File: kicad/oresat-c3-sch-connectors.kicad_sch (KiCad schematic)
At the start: 29 parts, among them J1 J-SAMTEC-TFM-120-01-L-D-RA, J2 J-TE-Debug-2-1734592-0, J3 J-MOLEX-SMPM-73300-003X, J4 J-MOLEX-SMPM-73300-003X

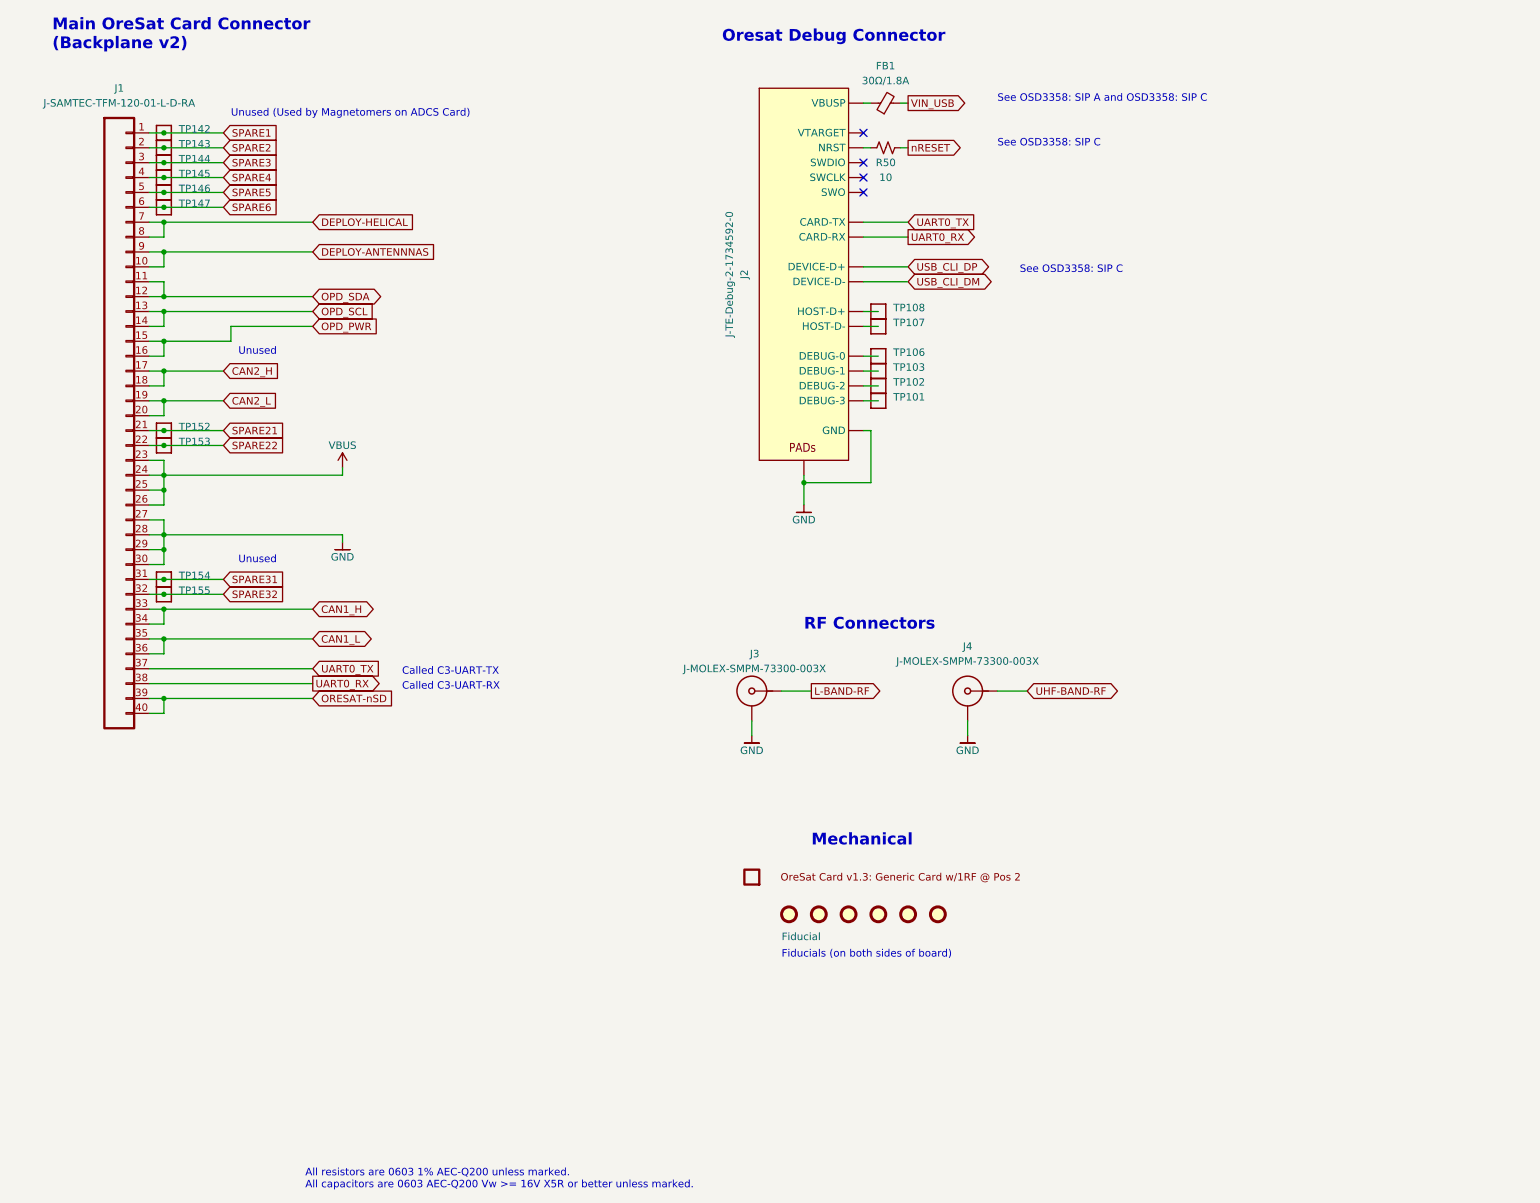
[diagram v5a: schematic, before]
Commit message: Updated all footprints for sheet one of the schematic.
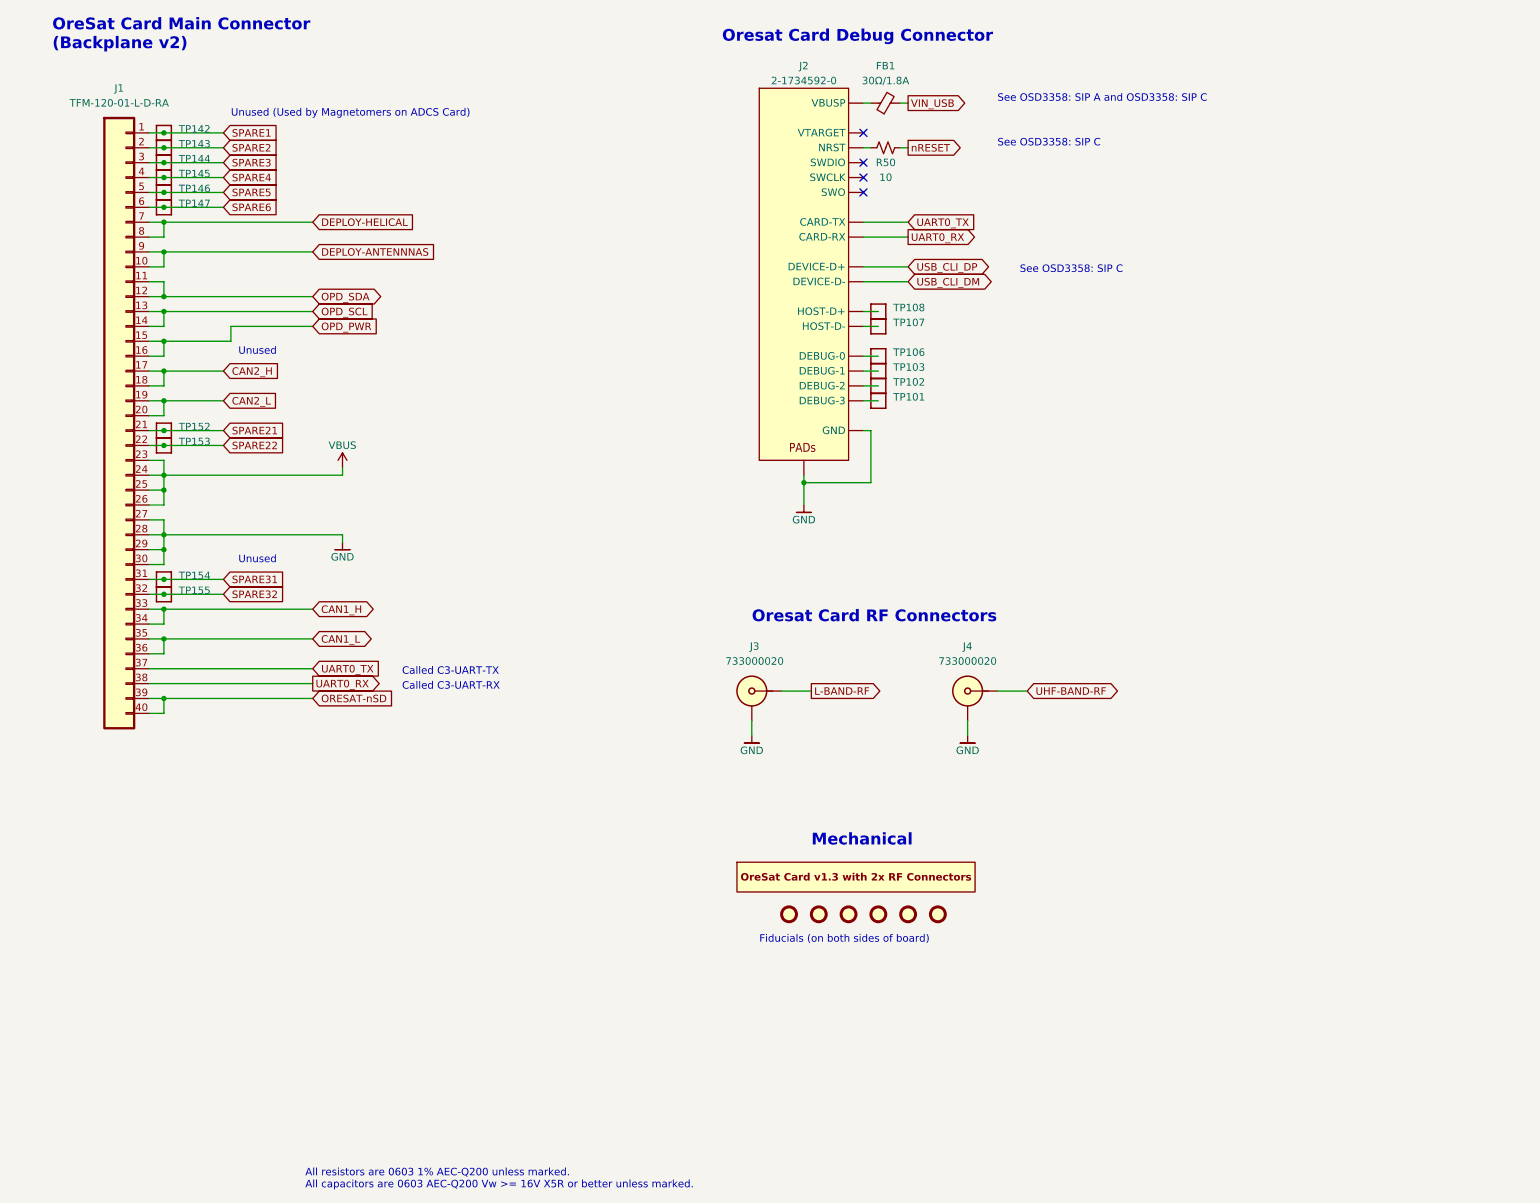
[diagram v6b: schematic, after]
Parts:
- J1: value J-SAMTEC-TFM-120-01-L-D-RA -> TFM-120-01-L-D-RA; footprint oresat-footprints:J-SAMTEC-TFM-120-X1-XXX-D-RA -> oresat-connectors:J-SAMTEC-TFM-120-X1-XXX-D-RA
- J2: value J-TE-Debug-2-1734592-0 -> 2-1734592-0; footprint oresat-footprints:J-TE_2-1734592-0 -> oresat-connectors:J-TE-2-1734592-0; symbol oresat-connectors:J-TE-Debug-2-1734592-0 -> oresat-connectors:J-TE-2-1734592-0
- J3, J4: value J-MOLEX-SMPM-73300-003X -> 733000020; symbol oresat-connectors:J-MOLEX-SMPM-73300-003X -> oresat-connectors:J-MOLEX-SMPM-73300-002X
- PCB1: footprint OreSat-Cards:ORESAT-CARD-V1.3-GENERIC-1RF-POS2 -> oresat-pcbs:ORESAT-CARD-V1.3-2RF-RIGHT; symbol OreSat-Cards:ORESAT-CARD-V1.3-GENERIC-1RF-POS2 -> oresat-pcbs:ORESAT-CARD-V1.3-2RF-RIGHT; now in the parts list
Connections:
- net GND: now also J3.SHEILD (SHIELD), J4.SHEILD (SHIELD); no longer J3.GND (SHIELD3), J4.GND (SHIELD3)
- net L-BAND-RF: now also J3.SIGNAL; no longer J3.RF (CENTER)
- net UHF-BAND-RF: now also J4.SIGNAL; no longer J4.RF (CENTER)
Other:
- note added: "OreSat Card Main Connector (Backplane v2)"
- note added: "Oresat Card Debug Connector"
- note added: "Oresat Card RF Connectors"
- note removed: "Main OreSat Card Connector (Backplane v2)"
- note removed: "Oresat Debug Connector"
- note removed: "RF Connectors"
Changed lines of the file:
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@@
     (stroke (width 0) (type default))
   )
-  (text "RF Connectors" (at 200.66 166.37 0)
+  (text "Oresat Card RF Connectors" (at 191.77 165.1 0)
     (effects (font (size 2 2) (thickness 0.4) bold) (justify left bottom))
   )
@@
     (effects (font (size 1.27 1.27)) (justify left bottom))
   )
-  (text "Main OreSat Card Connector\n(Backplane v2)" (at 72.39 67.31 0)
+  (text "OreSat Card Main Connector\n(Backplane v2)" (at 72.39 67.31 0)
     (effects (font (size 2 2) (thickness 0.4) bold) (justify left bottom))
   )
-  (text "Fiducials (on both sides of board)" (at 196.85 222.25 0)
+  (text "Fiducials (on both sides of board)" (at 193.04 219.71 0)
     (effects (font (size 1.27 1.27)) (justify left bottom))
   )
@@
     (effects (font (size 1.27 1.27)) (justify left bottom))
   )
-  (text "Oresat Debug Connector" (at 186.69 66.04 0)
+  (text "Oresat Card Debug Connector" (at 186.69 66.04 0)
     (effects (font (size 2 2) (thickness 0.4) bold) (justify left bottom))
   )
@@
     )
   )
-  (symbol (lib_id "oresat-connectors:J-TE-Debug-2-1734592-0") (at 200.66 104.14 0) (unit 1)
-    (in_bom yes) (on_board yes) (dnp no) (fields_autoplaced)
-    (property "Reference" "J2" (at 190.5 105.41 90)
-      (effects (font (size 1.27 1.27)))
-    )
-    (property "Value" "J-TE-Debug-2-1734592-0" (at 187.96 105.41 90)
-      (effects (font (size 1.27 1.27)))
-    )
-    (property "Footprint" "oresat-footprints:J-TE_2-1734592-0" (at 200.66 62.23 0)
-      (effects (font (size 1.27 1.27)) hide)
-    )
-    (property "Datasheet" "" (at 200.66 95.25 0)
+  (symbol (lib_id "oresat-connectors:J-TE-2-1734592-0") (at 200.66 104.14 0) (unit 1)
+    (in_bom yes) (on_board yes) (dnp no)
+    (property "Reference" "J2" (at 200.66 69.85 0)
+      (effects (font (size 1.27 1.27)))
+    )
+    (property "Value" "2-1734592-0" (at 200.66 72.39 0)
+      (effects (font (size 1.27 1.27)))
+    )
+    (property "Footprint" "oresat-connectors:J-TE-2-1734592-0" (at 200.66 62.23 0)
+      (effects (font (size 1.27 1.27)) hide)
+    )
+    (property "Datasheet" "https://www.te.com/usa-en/product-2-1734592-0.datasheet.pdf" (at 200.66 59.69 0)
       (effects (font (size 1.27 1.27)) hide)
     )
@@
     )
   )
-  (symbol (lib_id "oresat-connectors:J-MOLEX-SMPM-73300-003X") (at 191.77 176.53 0) (unit 1)
+  (symbol (lib_id "oresat-connectors:J-MOLEX-SMPM-73300-002X") (at 191.77 176.53 0) (unit 1)
     (in_bom yes) (on_board yes) (dnp no) (fields_autoplaced)
-    (property "Reference" "J3" (at 192.2526 170.18 0)
-      (effects (font (size 1.27 1.27)))
-    )
-    (property "Value" "J-MOLEX-SMPM-73300-003X" (at 192.2526 172.72 0)
-      (effects (font (size 1.27 1.27)))
-    )
-    (property "Footprint" "oresat-connectors:J-MOLEX-SMPM-073300-003X" (at 191.77 176.53 0)
-      (effects (font (size 1.27 1.27)) hide)
-    )
-    (property "Datasheet" "" (at 191.77 176.53 0)
-      (effects (font (size 1.27 1.27)) hide)
-    )
-    (pin "GND")
-    (pin "RF")
+    (property "Reference" "J3" (at 192.2526 168.91 0)
+      (effects (font (size 1.27 1.27)))
+    )
+    (property "Value" "733000020" (at 192.2526 171.45 0)
+      (effects (font (size 1.27 1.27)))
+    )
+    (property "Footprint" "oresat-connectors:J-MOLEX-SMPM-073300-003X" (at 191.77 170.18 0)
+      (effects (font (size 1.27 1.27)) hide)
+    )
+    (property "Datasheet" "https://tools.molex.com/pdm_docs/sd/733000020_sd.pdf" (at 191.77 167.64 0)
+      (effects (font (size 1.27 1.27)) hide)
+    )
+    (pin "SHEILD")
+    (pin "SIGNAL")
     (instances
       (project "oresat-c3"
@@
     )
   )
-  (symbol (lib_id "OreSat-Cards:ORESAT-CARD-V1.3-GENERIC-1RF-POS2") (at 191.77 208.28 0) (unit 1)
-    (in_bom no) (on_board yes) (dnp no) (fields_autoplaced)
-    (property "Reference" "PCB1" (at 191.77 204.47 0)
-      (effects (font (size 1.27 1.27)) hide)
-    )
-    (property "Value" "ORESAT-CARD-V1.3-GENERIC-1RF-POS2" (at 191.77 205.74 0)
-      (effects (font (size 1.27 1.27)) hide)
-    )
-    (property "Footprint" "OreSat-Cards:ORESAT-CARD-V1.3-GENERIC-1RF-POS2" (at 191.77 208.28 0)
-      (effects (font (size 1.27 1.27)) hide)
-    )
-    (property "Datasheet" "" (at 191.77 208.28 0)
+  (symbol (lib_id "oresat-pcbs:ORESAT-CARD-V1.3-2RF-RIGHT") (at 209.55 208.28 0) (unit 1)
+    (in_bom yes) (on_board yes) (dnp no) (fields_autoplaced)
+    (property "Reference" "PCB1" (at 209.55 204.47 0)
+      (effects (font (size 1.27 1.27)) hide)
+    )
+    (property "Value" "ORESAT-CARD-V1.3-GENERIC-1RF-POS2" (at 209.55 205.74 0)
+      (effects (font (size 1.27 1.27)) hide)
+    )
+    (property "Footprint" "oresat-pcbs:ORESAT-CARD-V1.3-2RF-RIGHT" (at 209.55 196.85 0)
+      (effects (font (size 1.27 1.27)) hide)
+    )
+    (property "Datasheet" "" (at 209.55 208.28 0)
       (effects (font (size 1.27 1.27)) hide)
     )
@@
     )
   )
-  (symbol (lib_id "oresat-connectors:J-MOLEX-SMPM-73300-003X") (at 228.6 176.53 0) (unit 1)
+  (symbol (lib_id "oresat-connectors:J-MOLEX-SMPM-73300-002X") (at 228.6 176.53 0) (unit 1)
     (in_bom yes) (on_board yes) (dnp no) (fields_autoplaced)
     (property "Reference" "J4" (at 228.6 168.91 0)
       (effects (font (size 1.27 1.27)))
     )
-    (property "Value" "J-MOLEX-SMPM-73300-003X" (at 228.6 171.45 0)
-      (effects (font (size 1.27 1.27)))
-    )
-    (property "Footprint" "oresat-connectors:J-MOLEX-SMPM-073300-003X" (at 228.6 176.53 0)
-      (effects (font (size 1.27 1.27)) hide)
-    )
-    (property "Datasheet" "" (at 228.6 176.53 0)
-      (effects (font (size 1.27 1.27)) hide)
-    )
-    (pin "GND")
-    (pin "RF")
+    (property "Value" "733000020" (at 228.6 171.45 0)
+      (effects (font (size 1.27 1.27)))
+    )
+    (property "Footprint" "oresat-connectors:J-MOLEX-SMPM-073300-003X" (at 228.6 170.18 0)
+      (effects (font (size 1.27 1.27)) hide)
+    )
+    (property "Datasheet" "https://tools.molex.com/pdm_docs/sd/733000020_sd.pdf" (at 228.6 167.64 0)
+      (effects (font (size 1.27 1.27)) hide)
+    )
+    (pin "SHEILD")
+    (pin "SIGNAL")
     (instances
       (project "oresat-c3"
@@
       (effects (font (size 1.27 1.27)))
     )
-    (property "Value" "J-SAMTEC-TFM-120-01-L-D-RA" (at 83.82 76.2 0)
-      (effects (font (size 1.27 1.27)))
-    )
-    (property "Footprint" "oresat-footprints:J-SAMTEC-TFM-120-X1-XXX-D-RA" (at 83.82 129.54 0)
-      (effects (font (size 1.27 1.27)) hide)
-    )
-    (property "Datasheet" "" (at 83.82 129.54 0)
+    (property "Value" "TFM-120-01-L-D-RA" (at 83.82 76.2 0)
+      (effects (font (size 1.27 1.27)))
+    )
+    (property "Footprint" "oresat-connectors:J-SAMTEC-TFM-120-X1-XXX-D-RA" (at 83.82 129.54 0)
+      (effects (font (size 1.27 1.27)) hide)
+    )
+    (property "Datasheet" "https://suddendocs.samtec.com/catalog_english/tfm.pdf" (at 83.82 129.54 0)
       (effects (font (size 1.27 1.27)) hide)
     )
@@
     )
     (property "Value" "Fiducial" (at 196.85 218.44 0)
-      (effects (font (size 1.27 1.27)) (justify left))
+      (effects (font (size 1.27 1.27)) (justify left) hide)
     )
     (property "Footprint" "oresat-misc:FIDUCIAL-1.0X2.0" (at 198.12 214.63 0)

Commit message: Try harder with sheet 1 footprints. Import sheet 1 footprints over, and then fix all the things on sheet 1 that break. New card better card outline, all connectors roughly placed.
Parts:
- J3, J4: footprint oresat-connectors:J-MOLEX-SMPM-073300-003X -> oresat-connectors:J-MOLEX-SMPM-073300-002X
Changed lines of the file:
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@@
     )
   )
-  (symbol (lib_id "oresat-connectors:J-MOLEX-SMPM-73300-002X") (at 191.77 176.53 0) (unit 1)
+  (symbol (lib_name "J-MOLEX-SMPM-73300-002X_1") (lib_id "oresat-connectors:J-MOLEX-SMPM-73300-002X") (at 191.77 176.53 0) (unit 1)
     (in_bom yes) (on_board yes) (dnp no) (fields_autoplaced)
     (property "Reference" "J3" (at 192.2526 168.91 0)
@@
       (effects (font (size 1.27 1.27)))
     )
-    (property "Footprint" "oresat-connectors:J-MOLEX-SMPM-073300-003X" (at 191.77 170.18 0)
+    (property "Footprint" "oresat-connectors:J-MOLEX-SMPM-073300-002X" (at 191.77 170.18 0)
       (effects (font (size 1.27 1.27)) hide)
     )
@@
       (effects (font (size 1.27 1.27)))
     )
-    (property "Footprint" "oresat-connectors:J-MOLEX-SMPM-073300-003X" (at 228.6 170.18 0)
-      (effects (font (size 1.27 1.27)) hide)
-    )
+    (property "Footprint" "oresat-connectors:J-MOLEX-SMPM-073300-002X" (at 228.6 170.18 0)
+      (effects (font (size 1.27 1.27)) hide)
+    )

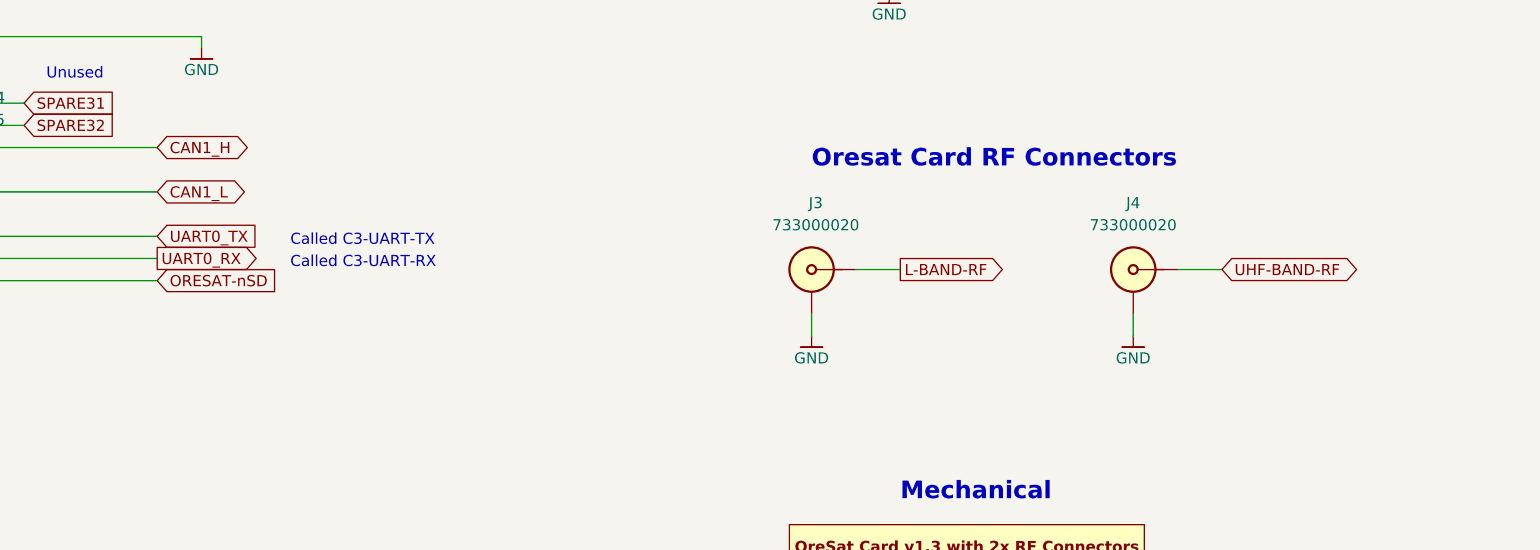
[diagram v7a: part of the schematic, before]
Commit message: Big C3 cleanup with Glenn; radios off of one SPS + separate LDOs, removed lots of test 0 ohm resistors, cleaned up capacitance, and finally wired everything up to the octavo. ZERO ERC errors.
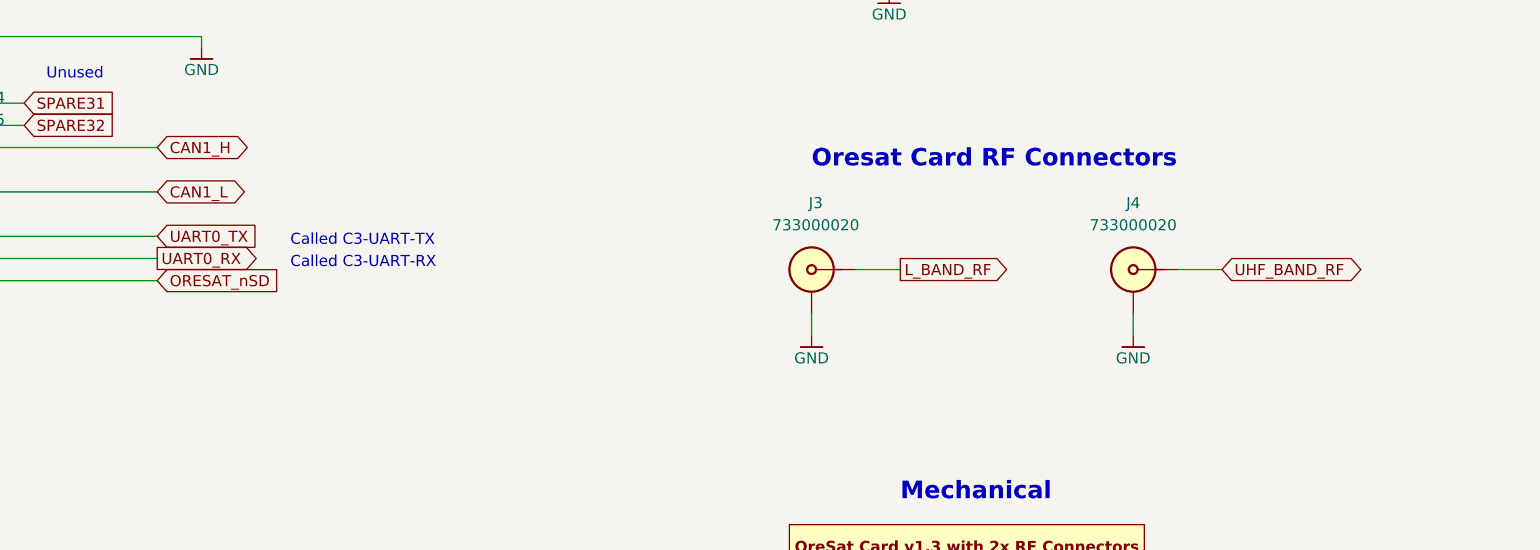
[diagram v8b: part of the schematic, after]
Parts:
- TP101, TP102, TP103, TP106, TP107, TP108, TP142, TP143, TP144, TP145, TP146, TP147, TP152, TP153, TP154, TP155: footprint oresat-misc:PAD.03X.04 -> TestPoint:TestPoint_Pad_D1.0mm; symbol oresat-misc:Test-Point -> oresat-misc:Test-Point-1mm-round
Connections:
- net L-BAND-RF renamed L_BAND_RF
- net ORESAT-nSD renamed ORESAT_nSD
- net UHF-BAND-RF renamed UHF_BAND_RF
